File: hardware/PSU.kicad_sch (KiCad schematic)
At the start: 0 parts

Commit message: feat(hardware): Move PSU to subschematic
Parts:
- added C1: 470pF, symbol Device:C
- added C21, C5: 2.2uF, symbol Device:C
- added C22: 1.0 uF, symbol Device:C
- added C23, C24, C25: 2.2 uF, symbol Device:C
- added D1: D_Schottky, symbol Device:D_Schottky
- added J1: UJ20-C-H-G-SMT-2A-P16-TR, UJ20-C-H-G-SMT-1-P16-TR:SAMESKY_UJ20-C-H-G-SMT-1-P16-TR, symbol UJ20-C-H-G-SMT-1-P16-TR:UJ20-C-H-G-SMT-1-P16-TR
- added R1, R9: 5.1k, symbol Device:R
- added R10, R12: 174k, symbol Device:R
- added R11, R13: 100k, symbol Device:R
- added U2: MIC5205-3.3YM5, Package_TO_SOT_SMD:SOT-23-5, symbol Regulator_Linear:MIC5205-3.3YM5
- added U4: LM27762, Package_SON:WSON-12-1EP_3x2mm_P0.5mm_EP1x2.65_ThermalVias, symbol Regulator_SwitchedCapacitor:LM27762
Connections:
- new net: R12.1, R13.2, U4.7 (FB-)
- new net: C1.1, U2.4 (BP)
- new net: C5.1, U4.5 (CP)
- new net: C22.1, U4.10 (C+)
- new net: C22.2, U4.9 (C-)
- new net: R10.2, R11.2, U4.2 (FB+)
- new net +3.3VA: C23.1, R10.1, U4.11 (OUT+)
- new net +3V3: C21.1, U2.5 (OUT)
- new net -3V3: C24.1, R12.2, U4.6 (OUT-)
- new net GND: C1.2, C21.2, C23.2, C24.2, C25.2, C5.2, J1.A1_B12 (GND), J1.B1_A12 (GND), J1.SH1 (SHIELD), J1.SH2 (SHIELD), J1.SH3 (SHIELD), J1.SH4 (SHIELD), R1.2, R11.1, R13.1, R9.2, U2.2 (GND), U4.1 (PGOOD), U4.13 (PAD), U4.4 (GND)
- new net UCB_CC1: R1.1
- new net USB_CC1: J1.A5 (CC1)
- new net USB_CC2: J1.B5 (CC2), R9.1
- new net USB_D+: J1.A6 (DP1), J1.B6 (DP2)
- new net USB_D-: J1.A7 (DN1), J1.B7 (DN2)
- new net VBUS: D1.2 (A), J1.A4_B9 (VBUS), J1.B4_A9 (VBUS)
- new net VSYS: C25.1, D1.1 (K), U2.1 (IN), U2.3 (EN), U4.12 (EN+), U4.3 (VIN), U4.8 (EN-)
- no-connect marks 0 -> 2
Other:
- note added: "Placeholder schottky diode. This will be replaced by the USB isolator"
- note added: "Power"
- note added: "Power for Digital Components. Input voltage range from 2.5V to 16V (from USB C) with a fixed output of 3.3V."
- note added: "Power for analog component. This is assuming that VSYS is going to be a 5V input otherwise resistor values will have to be adjusted for the feedback loop. Can take an input voltage range of 2.7V to 5.5V. Can output with a range of +-1.5V to +-5.5V"
- note added: "Pull down resistors on CC pins configure usb c in client mode"
- note added: "USB C"

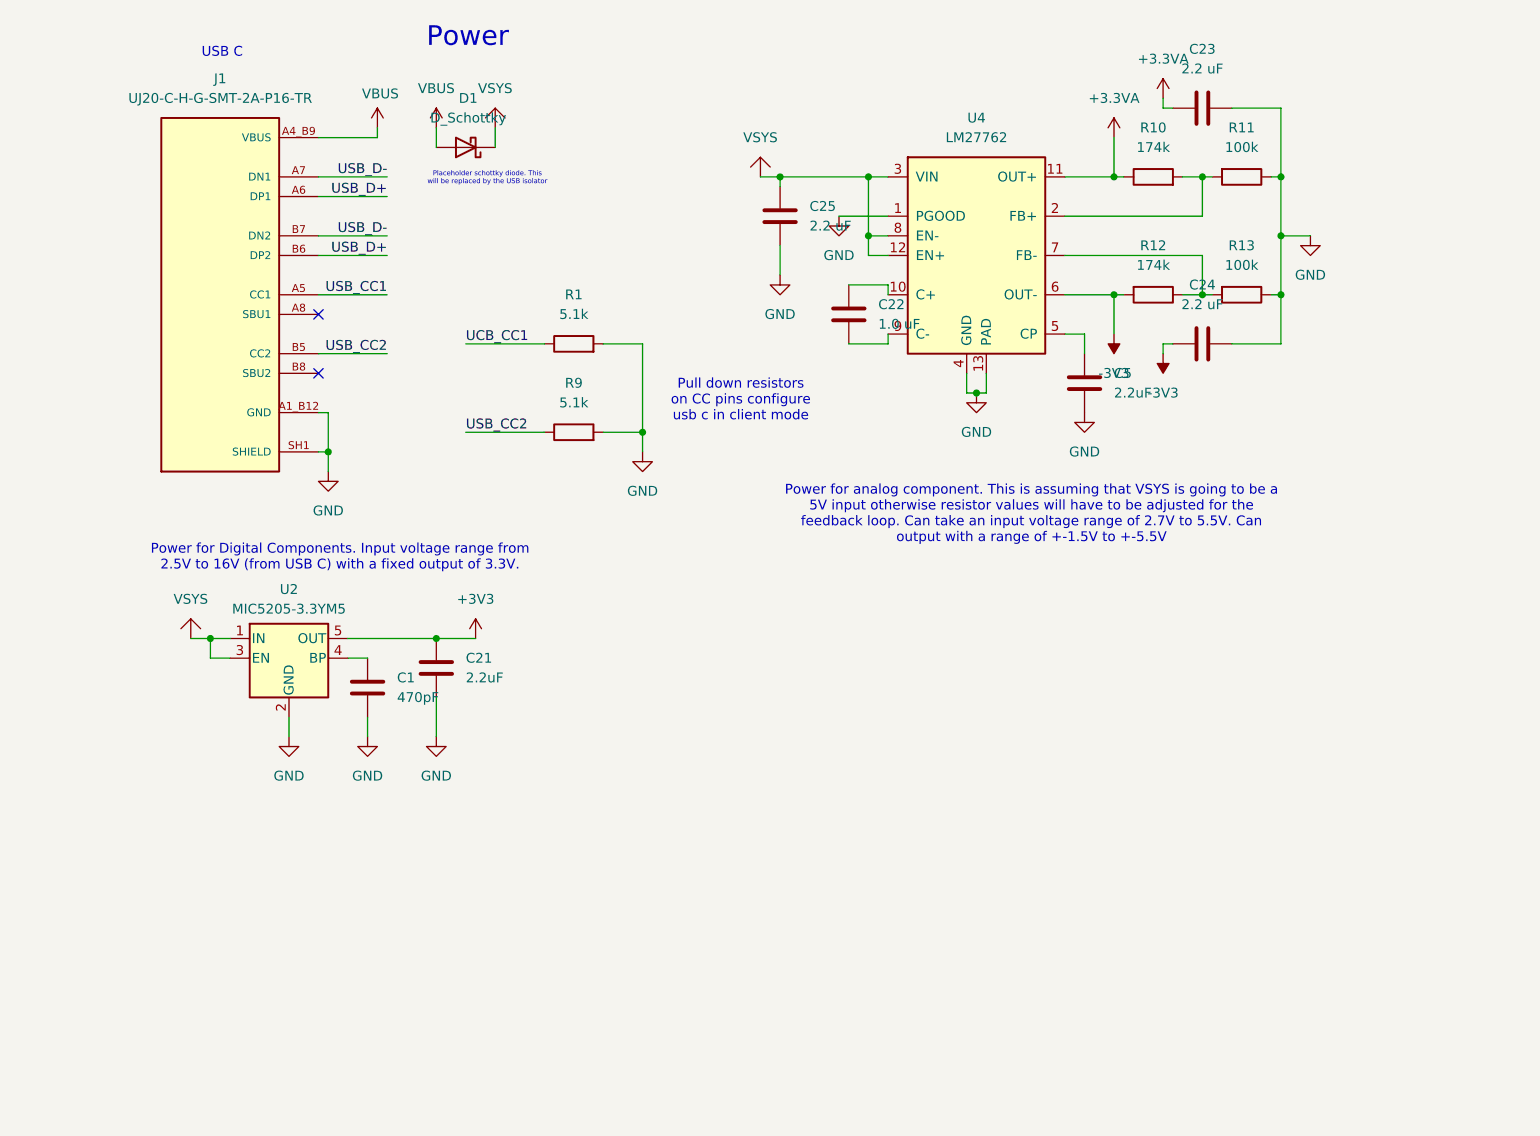
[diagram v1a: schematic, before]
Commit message: not done with Vref just saving for the night
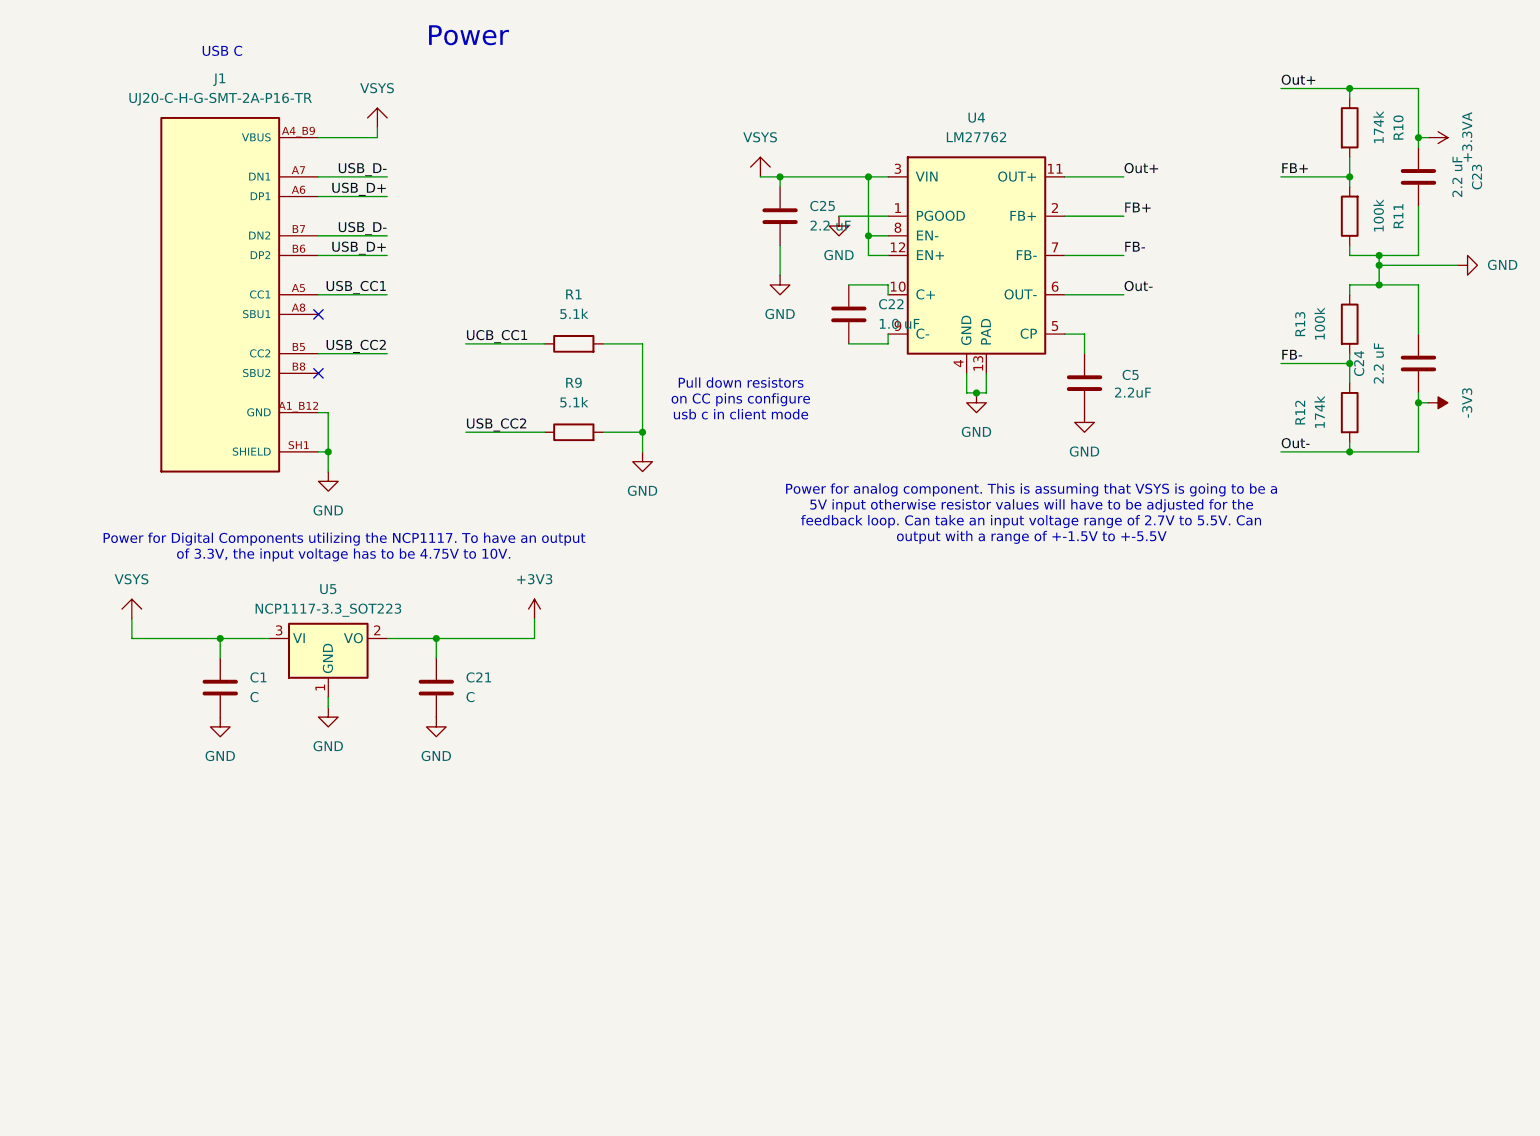
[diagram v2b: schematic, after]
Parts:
- removed D1: D_Schottky, symbol Device:D_Schottky
- removed U2: MIC5205-3.3YM5, Package_TO_SOT_SMD:SOT-23-5, symbol Regulator_Linear:MIC5205-3.3YM5
- added U5: NCP1117-3.3_SOT223, Package_TO_SOT_SMD:SOT-223-3_TabPin2, symbol Regulator_Linear:NCP1117-3.3_SOT223
- C1: value 470pF -> C
- C21: value 2.2uF -> C
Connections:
- net VBUS is gone; now on net VSYS: J1.A4_B9 (VBUS), J1.B4_A9 (VBUS)
- net +3V3: now also U5.2 (VO)
- net GND: now also U5.1 (GND)
- net VSYS: now also C1.1, U5.3 (VI)
- net FB-: now reaches R12.1, R13.2, U4.7 (FB-)
- net FB+: now reaches R10.2, R11.2, U4.2 (FB+)
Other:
- note added: "Power for Digital Components utilizing the NCP1117. To have an output of 3.3V, the input voltage has to be 4.75V to 10V."
- note removed: "Placeholder schottky diode. This will be replaced by the USB isolator"
- note removed: "Power for Digital Components. Input voltage range from 2.5V to 16V (from USB C) with a fixed output of 3.3V."
- moved on the sheet: C23, C24, R10, R11, R12, R13

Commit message: updating
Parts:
- added C26: 0.1 uF, symbol Device:C
- added C27: 1 uF, symbol Device:C
- added U2: REF35330QDBVR, Package_TO_SOT_SMD:SOT-23-6, symbol Reference_Voltage:REF35330QDBVR
- R10: value 174k -> 18.7k
- R11, R13: value 100k -> 50k
- R12: value 174k -> 17.8k
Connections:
- net GND: now also C26.2, C27.1, U2.1 (GND), U2.2 (GND)
- net VSYS: now also C26.1, U2.3 (EN), U2.4 (VIN)
- net +3.3VA renamed +1V65
- net -3V3 renamed -1V65
- new net: C27.2, U2.5 (NR)
- new net VREF: U2.6 (VREF)
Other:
- note added: "Voltage reference point. I will take an input voltage from the USB C and output a 3.3V voltage ref. Capacitors are there to further filter out any noise but the IC itself is already supplies incredibly clean voltage."
